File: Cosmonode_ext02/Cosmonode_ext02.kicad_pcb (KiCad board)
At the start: 2 copper layers, 24.1 x 33 mm, 19 parts, among them J1 CONN_01X04, J2 CONN_01X04, J3 CONN_01X08, J4 CONN_01X08, J5 GS3, J6 GS3, Q1 BSS138, Q2 BSS138, SW1 SW_Push, SW2 SW_Push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

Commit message: big push!
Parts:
- added J7: Aloes_Logo, Aloes:Aloes_mini, F.Cu at (175.3, 104.8)
- moved J3 29.2 mm to (158.8, 120.7)
- moved J4 29.2 mm to (158.8, 91.4)
- moved J5 3.18 mm to (158.8, 95.2)
- moved J6 2.54 mm to (165.7, 95.2)
- moved U1 2.54 mm to (172.7, 95.9), turned to 0 degrees
- moved J2 1.42 mm to (158.8, 108.6)
- moved J1 1.27 mm to (158.8, 100.3)
- moved Q1 0.64 mm to (158.8, 115.6)
- moved Q2 0.64 mm to (165.7, 115.6)
- moved SW1 0.64 mm to (176.5, 100.3)
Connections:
- net Net-(J3-Pad8) renamed /A6
- net Net-(J4-Pad8) renamed /A7
- J1 pad 1: Net-(C1-Pad2) -> +5V
- J1 pad 2: Net-(C1-Pad1) -> /D3_5V
- J1 pad 3: /D3_5V -> Net-(C1-Pad1)
- J1 pad 4: +5V -> Net-(C1-Pad2)
- J2 pad 1: Net-(C5-Pad2) -> +5V
- J2 pad 2: Net-(C1-Pad1) -> /D4_5V
- J2 pad 3: /D4_5V -> Net-(C1-Pad1)
- J2 pad 4: +5V -> Net-(C5-Pad2)
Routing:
- net Net-(C1-Pad1): track 83.8 -> 28.3 mm, vias 1 -> 6
- net /D6: track 4.07 -> 54.3 mm
- net /D5: track 5.32 -> 31.7 mm
- net /D3_5V: track 50.7 -> 26.5 mm
- net GND: track 31.0 -> 6.86 mm
- net /D4: track 29.1 -> 5.77 mm
- net /D3: track 27.8 -> 4.75 mm
- net +3V3: track 41.8 -> 55.2 mm, vias 1 -> 0
- net +5V: track 43.9 -> 54.4 mm, vias 1 -> 0
- net Net-(C5-Pad2): track 22.1 -> 12.9 mm, vias 2 -> 0
- net Net-(C1-Pad2): track 32.0 -> 23.2 mm, vias 1 -> 0
- net Net-(J5-Pad2): track 18.2 -> 16.6 mm
- net /D4_5V: track 13.4 -> 14.3 mm
- added copper zone on F.Cu, net Net-(C1-Pad1)
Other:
- board size 24.1 x 33 mm -> 24.1 x 34.3 mm
- board text added: "+3V3"
- board text added: "A0"
- board text added: "A1"
- board text added: "A4"
- board text added: "A5"
- board text added: "A6"
- board text added: "A7"
- board text added: "ALOES.IO"
- board text added: "BAT+"
- board text added: "D3"
- board text added: "D4"
- board text added: "D5"
- board text added: "D6"
- board text added: "D7"
- board text added: "GND"

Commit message: big push2
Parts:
- added J8: OSHW_Logo, Symbols:OSHW-Logo_5.7x6mm_SilkScreen, B.Cu at (160.7, 95.9)
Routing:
- net Net-(C1-Pad1): track 28.3 -> 0.00 mm, vias 6 -> 0
- net +3V3: track 55.2 -> 36.7 mm
- net /D6: track 54.3 -> 36.1 mm, vias 0 -> 1
- net Net-(J5-Pad2): track 16.6 -> 22.6 mm
- net /D5: track 31.7 -> 35.2 mm
- net +5V: track 54.4 -> 54.9 mm
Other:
- board text added: "Extension #2 Liquid Level XKC-Y25 sensor"

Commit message: update to V0.7 (WIP)
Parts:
- J3, J4: value CONN_01X08 -> CONN_01X12; footprint Pin_Headers:Pin_Header_Straight_1x08_Pitch2.54mm -> Socket_Strips:Socket_Strip_Straight_1x12_Pitch2.54mm
- moved J4 34.2 mm to (176.5, 120.7), turned to 90 degrees
- moved J3 30.9 mm to (148.6, 91.4)
- moved J6 25.9 mm to (150.5, 116.2)
- moved J5 21.0 mm to (159.4, 116.2)
- moved Q1 20.8 mm to (150.5, 96.5), turned to 180 degrees
- moved U1 20.3 mm to (167.6, 115.6), turned to 180 degrees
- moved Q2 20.1 mm to (159.4, 96.5), turned to 180 degrees
- moved C1 18.7 mm to (173.4, 95.2)
- moved C2 18.7 mm to (173.4, 98.4)
- moved J8 14.7 mm to (175.3, 97.8), turned to 90 degrees
- moved J1 8.64 mm to (150.5, 102.9), turned to 270 degrees
- moved J7 8.03 mm to (177.8, 97.2), turned to 270 degrees
- moved C3 7.24 mm to (167.6, 98.4)
- moved C4 7.24 mm to (167.6, 95.2)
- moved C5 7.24 mm to (167.6, 101.6)
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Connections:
- net /A0 renamed A6
- net /A1 renamed A7
- net /A5 renamed D8
- net /A6 renamed RX
- net /A7 renamed D9
- net /BAT+ renamed +BATT
- net /D3 renamed A0
- net /D3_5V renamed A0_5V
- net /D4 renamed A1
- net /D4_5V renamed A1_5V
- net /D7 renamed A5
- J3 pad 3: /D5 -> A3
- J3 pad 4: /D6 -> A4
- J4 pad 3: +3V3 -> GND
- J4 pad 4: GND -> D5
- J4 pad 5: GND -> D6
- J4 pad 6: /A4 -> D7
- J5 pad 1: /D5 -> D7
- J6 pad 1: /D6 -> D6
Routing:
- net /D6: track 36.1 -> 0.00 mm, vias 1 -> 0
- net /D5: track 35.2 -> 0.00 mm
- net +3V3: track 36.7 -> 61.4 mm
- net Net-(C1-Pad2): track 23.6 -> 43.8 mm
- net D6: track 0.00 -> 19.8 mm
- net +5V: track 54.9 -> 73.5 mm
- net GND: track 6.86 -> 21.7 mm
- net Net-(J5-Pad2): track 22.6 -> 7.85 mm
- net Net-(C1-Pad1): track 0.00 -> 12.9 mm, vias 0 -> 12
- net D7: track 0.00 -> 9.91 mm, vias 0 -> 1
- net Net-(C5-Pad2): track 12.9 -> 22.6 mm
- net A0_5V: track 26.5 -> 35.1 mm, vias 1 -> 0
- net A1: track 5.77 -> 11.7 mm
- net A1_5V: track 14.3 -> 18.8 mm, vias 0 -> 1
- net A0: track 4.75 -> 6.23 mm
- added copper zone on B.Cu, net Net-(C1-Pad1)
- removed copper zone on F.Cu, net Net-(C1-Pad1)
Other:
- board size 24.1 x 34.3 mm -> 35.6 x 31.8 mm
- board text added: "A3"
- board text added: "D2"
- board text added: "D8"
- board text added: "D9"
- board text added: "MISO"
- board text added: "MOSI"
- board text added: "RST"
- board text added: "RX"
- board text added: "SCK"
- board text added: "TX"
- board text added: "^"

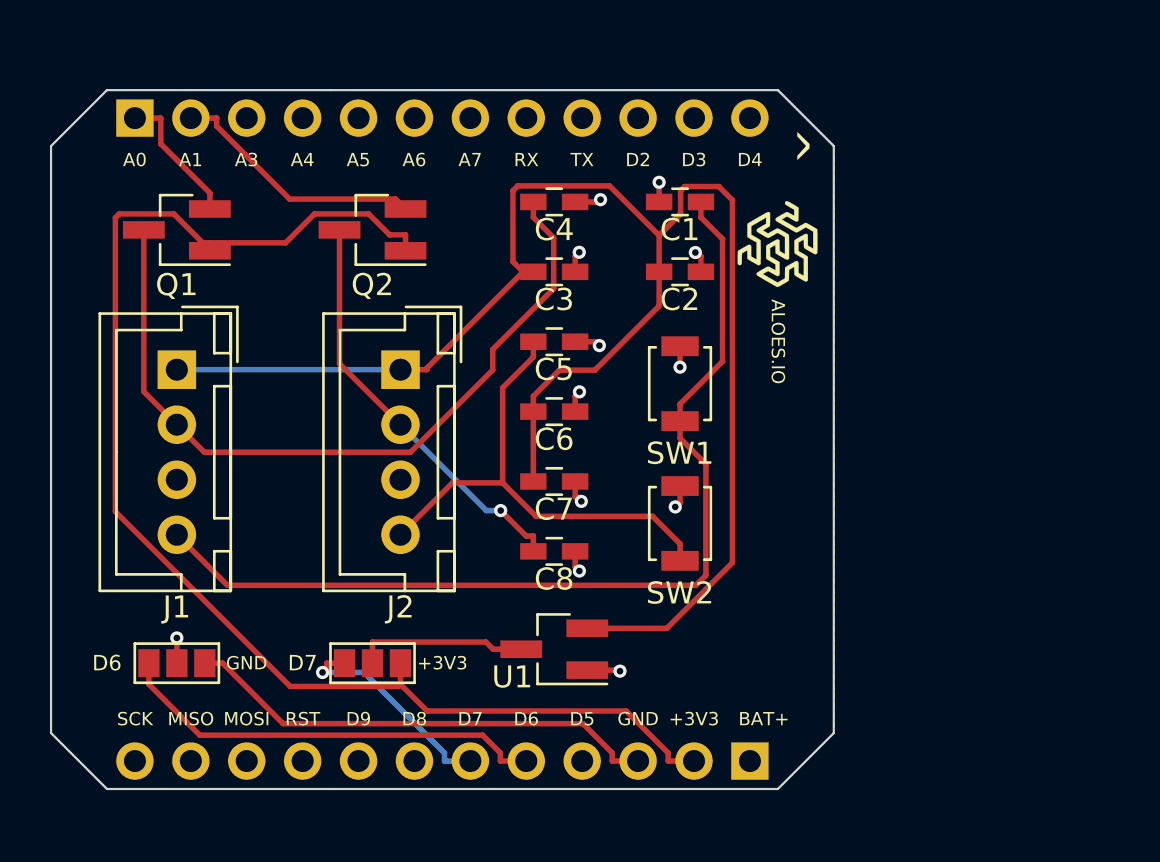
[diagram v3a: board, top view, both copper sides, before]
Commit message: near v0.7 ( mother and ext02 ), add mini extension
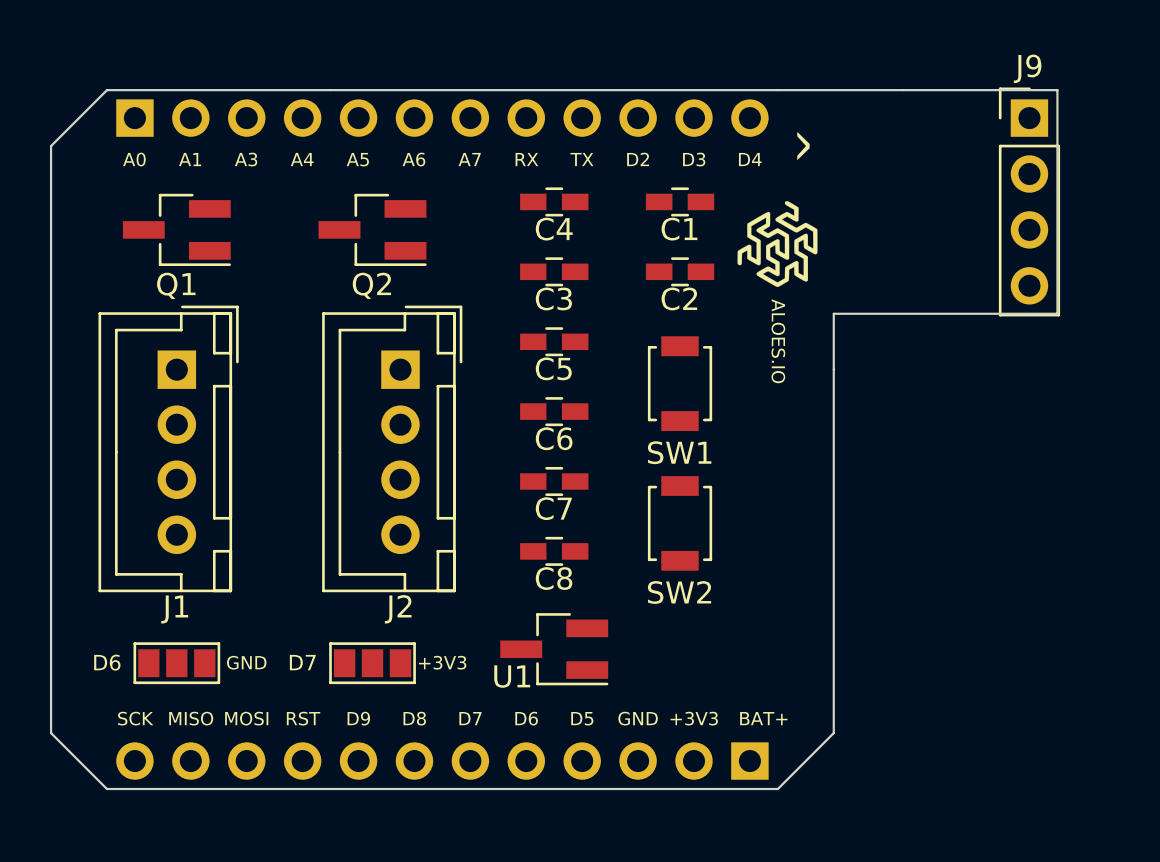
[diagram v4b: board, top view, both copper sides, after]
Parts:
- added J9: CONN_01X04, Socket_Strips:Socket_Strip_Straight_1x04_Pitch2.54mm, F.Cu at (189.2, 91.4)
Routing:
- net +5V: track 73.5 -> 0.00 mm
- net +3V3: track 61.4 -> 0.00 mm
- net Net-(C1-Pad2): track 43.8 -> 0.00 mm
- net A0_5V: track 35.1 -> 0.00 mm
- net Net-(C5-Pad2): track 22.6 -> 0.00 mm
- net GND: track 21.7 -> 0.00 mm
- net D6: track 19.8 -> 0.00 mm
- net A1_5V: track 18.8 -> 0.00 mm, vias 1 -> 0
- net Net-(C1-Pad1): track 12.9 -> 0.00 mm, vias 12 -> 0
- net A1: track 11.7 -> 0.00 mm
- net D7: track 9.91 -> 0.00 mm, vias 1 -> 0
- net Net-(J5-Pad2): track 7.85 -> 0.00 mm
- net A0: track 6.23 -> 0.00 mm
- removed copper zone on B.Cu, net Net-(C1-Pad1)
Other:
- board size 35.6 x 31.8 mm -> 45.7 x 31.8 mm

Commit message: fix and update
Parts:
- added J10: CONN_01X06, Pin_Headers:Pin_Header_Straight_1x06_Pitch2.54mm, F.Cu at (178.4, 97.8)
- moved J9 21.7 mm to (191.8, 113.0)
- moved J7 18.5 mm to (176.5, 115.6), turned to 0 degrees
- moved J1 0.63 mm to (151.1, 102.9)
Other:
- board size 45.7 x 31.8 mm -> 48.3 x 31.8 mm
- board text added: "+5V"
- board text added: "A0_5V"
- board text added: "A1_5V"
- board text added: "ADJ"
- board text added: "SCL"
- board text added: "SDA"
